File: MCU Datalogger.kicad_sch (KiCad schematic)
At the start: 0 parts

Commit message: imported all needed devices
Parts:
- added BT1: Battery, symbol Device:Battery
- added C1, C2, C3, C4: C, symbol Device:C
- added C5: C_Polarized, symbol Device:C_Polarized
- added D1, D2: LED, symbol Device:LED
- added H1, H2, H3, H4: MountingHole, symbol Mechanical:MountingHole
- added J1, J2: Conn_01x04_Pin, symbol Connector:Conn_01x04_Pin
- added J3: Conn_01x09_Pin, symbol Connector:Conn_01x09_Pin
- added J4: Conn_02x03_Odd_Even, symbol Connector_Generic:Conn_02x03_Odd_Even
- added R1, R2, R3, R4, R5, R6, R7: R, symbol Device:R
- added U1, U2: 24LC1025, symbol Memory_EEPROM:24LC1025
- added U3: ATmega328P-A, Package_QFP:TQFP-32_7x7mm_P0.8mm, symbol MCU_Microchip_ATmega:ATmega328P-A
- added U4: ds1337s+, 21-0041B_8_MXM, symbol 2026-08-13_06-12-53:ds1337s+
- added Y1, Y2: Crystal, symbol Device:Crystal
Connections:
- new net: U3.21 (GND), U3.3 (GND), U3.5 (GND)
- new net: U3.4 (VCC), U3.6 (VCC)
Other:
- company: (none) -> I love KiCAD inc
- title: (none) -> MCU Datalogger w EEPROM & CLK

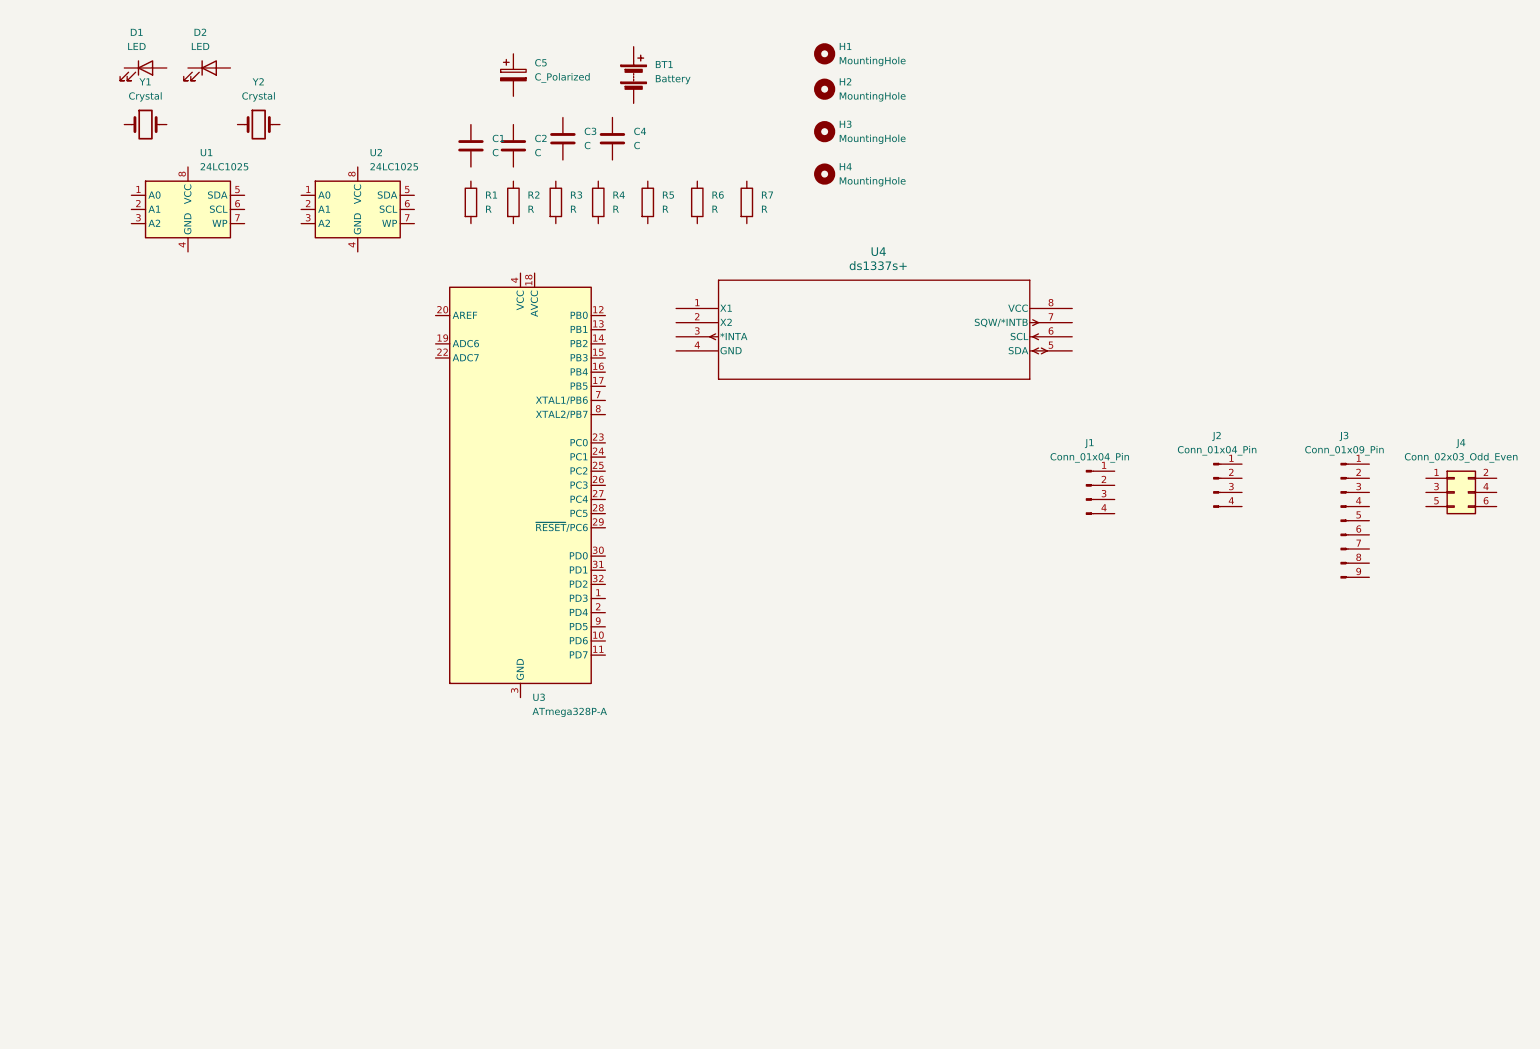
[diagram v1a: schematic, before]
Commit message: added footprints
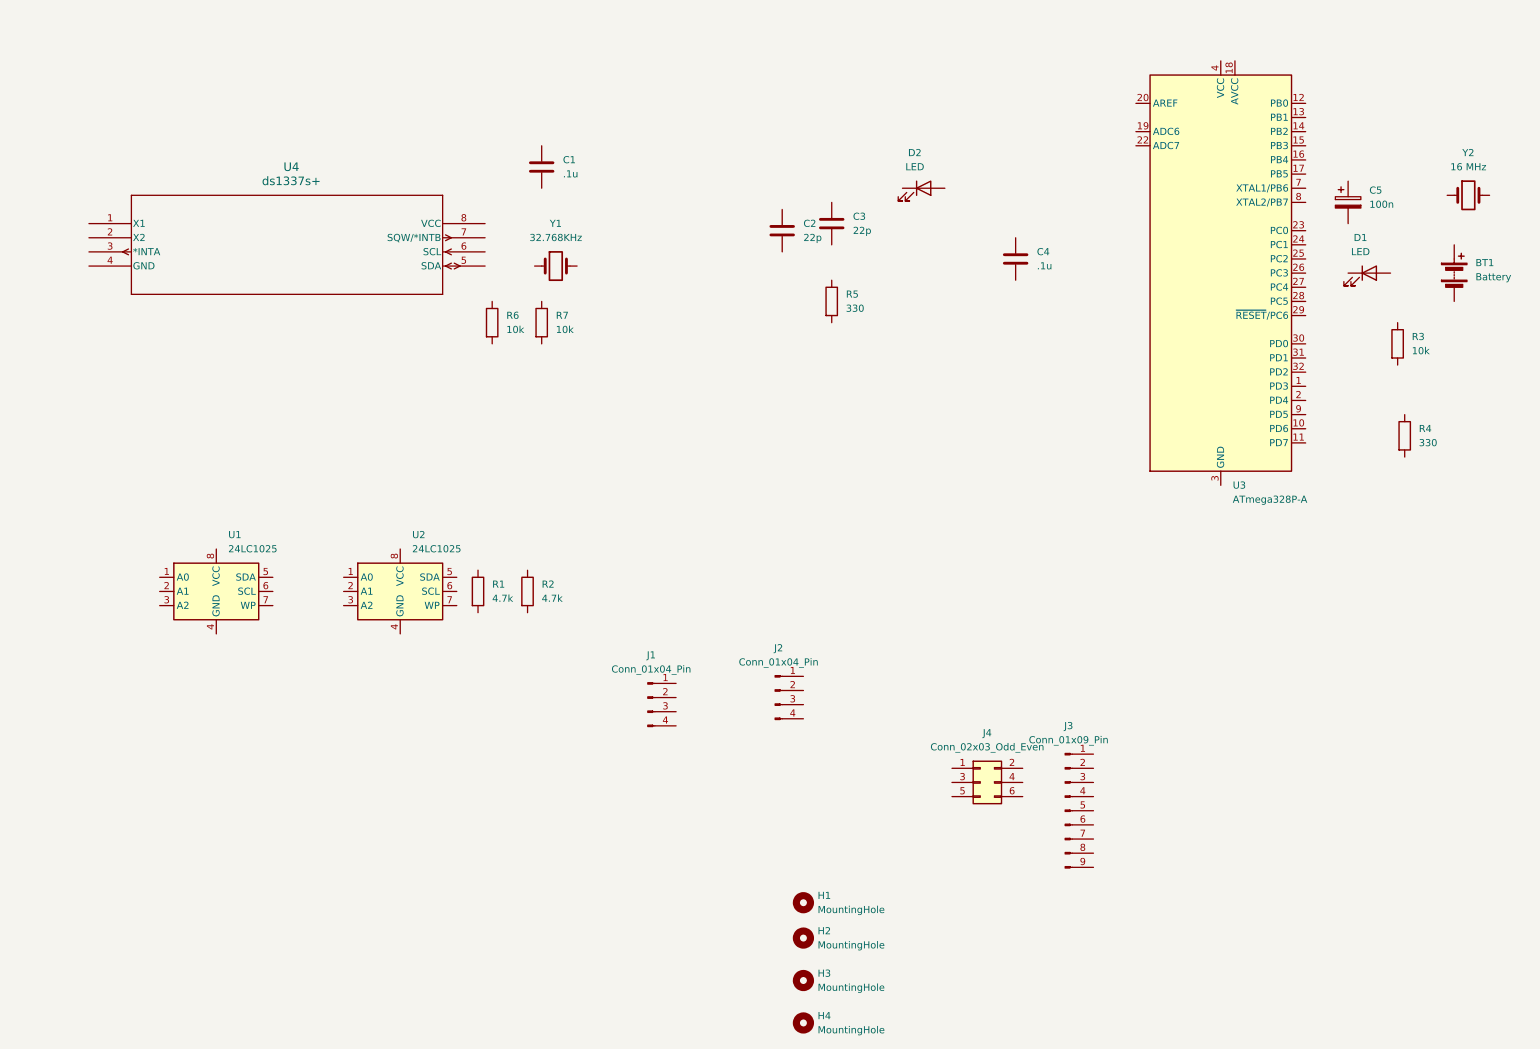
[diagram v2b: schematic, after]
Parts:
- BT1: footprint (none) -> Connector_PinHeader_2.54mm:PinHeader_1x02_P2.54mm_Vertical
- C1, C4: value C -> .1u; footprint (none) -> Capacitor_SMD:C_0805_2012Metric
- C2, C3: value C -> 22p; footprint (none) -> Capacitor_SMD:C_0805_2012Metric
- C5: value C_Polarized -> 100n; footprint (none) -> Capacitor_SMD:C_0805_2012Metric
- D1, D2: footprint (none) -> LED_SMD:LED_0805_2012Metric
- H1, H2, H3, H4: footprint (none) -> MountingHole:MountingHole_2.1mm
- J1, J2: footprint (none) -> Connector_PinHeader_2.54mm:PinHeader_1x04_P2.54mm_Vertical
- J3: footprint (none) -> Connector_PinHeader_2.54mm:PinHeader_1x09_P2.54mm_Vertical
- J4: footprint (none) -> Connector_PinHeader_2.54mm:PinHeader_2x03_P2.54mm_Vertical
- R1, R2: value R -> 4.7k; footprint (none) -> Resistor_SMD:R_0805_2012Metric
- R3, R6, R7: value R -> 10k; footprint (none) -> Resistor_SMD:R_0805_2012Metric
- R4, R5: value R -> 330; footprint (none) -> Resistor_SMD:R_0805_2012Metric
- U1, U2: footprint (none) -> Package_SO:SOIC-8_3.9x4.9mm_P1.27mm
- U4: footprint 21-0041B_8_MXM -> (none)
- Y1: value Crystal -> 32.768KHz; footprint (none) -> Crystal:Crystal_SMD_5032-2Pin_5.0x3.2mm_HandSoldering
- Y2: value Crystal -> 16 MHz; footprint (none) -> Crystal:Crystal_SMD_5032-2Pin_5.0x3.2mm_HandSoldering
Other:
- moved on the sheet: BT1, C1, C2, C3, C4, C5, D1, D2, H1, H2, H3, H4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

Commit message: scematic connections done mostly
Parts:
- removed R3: 10k, Resistor_SMD:R_0805_2012Metric, symbol Device:R
- added R8: 10k, Resistor_SMD:R_0805_2012Metric, symbol Device:R
- U4: footprint (none) -> footprints:21-0041B_8_MXM
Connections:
- net at D1.1 (K): now also R4.1
- net at D1.2 (A): now also BT1.1 (+), C5.1, U3.18 (AVCC), U3.4 (VCC), U3.6 (VCC)
- net at U4.1 (X1): now also Y1.1
- net at U4.2 (X2): now also Y1.2
- net at U4.3 (*INTA): now also R7.2
- net GND: now reaches U4.4 (GND)
- net GND: now also BT1.2 (-), C1.2, C2.2, C3.2, C4.2, C5.2, R4.2, R5.1, U1.4 (GND), U1.7 (WP), U2.2 (A1), U2.4 (GND), U2.7 (WP), U3.21 (GND), U3.3 (GND), U3.5 (GND)
- net SDA: now reaches U4.5 (SDA)
- net SDA: now also R2.2, U1.5 (SDA), U2.5 (SDA), U3.27 (PC4)
- net SCL: now reaches U4.6 (SCL)
- net SCL: now also R1.2, U1.6 (SCL), U2.6 (SCL)
- net at U4.7 (SQW/*INTB): now also R6.2
- net VCC: now reaches U4.8 (VCC)
- net VCC: now also C1.1, R1.1, R2.1, R6.1, R7.1, U1.1 (A0), U1.2 (A1), U1.3 (A2), U1.8 (VCC), U2.1 (A0), U2.3 (A2), U2.8 (VCC), R8.1
- net at Y2.1: now also C3.1, U3.8 (XTAL2/PB7)
- net at Y2.2: now also C2.1, U3.7 (XTAL1/PB6)
- net at D2.1 (K): now also R5.2
- net SCK: now reaches D2.2 (A)
- net SCK: now also U3.17 (PB5), U3.28 (PC5)
- net D3: now reaches U3.1 (PD3)
- net D6: now reaches U3.10 (PD6)
- net D7: now reaches U3.11 (PD7)
- net D8: now reaches U3.12 (PB0)
- net MOSI: now reaches U3.15 (PB3)
- net MISO: now reaches U3.16 (PB4)
- net D4: now reaches U3.2 (PD4)
- net at U3.20 (AREF): now also C4.1
- net RESET: now reaches U3.29 (~{RESET}/PC6)
- net RESET: now also R8.2
- net RX: now reaches U3.30 (PD0)
- net TX: now reaches U3.31 (PD1)
- net D2: now reaches U3.32 (PD2)
- net D5: now reaches U3.9 (PD5)
- no-connect marks 0 -> 8
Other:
- moved on the sheet: BT1, C1, C2, C3, C4, C5, D1, D2, J4, R1, R2, R4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

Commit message: done with labels and connections and net classes
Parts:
- removed J1, J2: Conn_01x04_Pin, Connector_PinHeader_2.54mm:PinHeader_1x04_P2.54mm_Vertical, symbol Connector:Conn_01x04_Pin
- removed J3: Conn_01x09_Pin, Connector_PinHeader_2.54mm:PinHeader_1x09_P2.54mm_Vertical, symbol Connector:Conn_01x09_Pin
- removed J4: Conn_02x03_Odd_Even, Connector_PinHeader_2.54mm:PinHeader_2x03_P2.54mm_Vertical, symbol Connector_Generic:Conn_02x03_Odd_Even
- removed U4: ds1337s+, footprints:21-0041B_8_MXM, symbol 2026-08-13_06-12-53:ds1337s+
- added U4: ds1337s+, footprints:21-0041B_8_MXM, symbol 2026-08-25_23-21-17:ds1337s+
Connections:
- net GND: now also U4.4 (GND)
- net SCL: now also U4.6 (SCL)
- net SDA: now also U4.5 (SDA)
- net VCC: now also BT1.1 (+), C5.1, D1.2 (A), U3.18 (AVCC), U3.4 (VCC), U3.6 (VCC), U4.8 (VCC)
- net at Y1.1: now also U4.1 (X1)
- net at Y1.2: now also U4.2 (X2)
- net at R7.2: now also U4.7 (SQW/*INTB)
- net at R6.2: now also U4.3 (*INTA)
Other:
- added sheet connectors (untitled.kicad_sch)

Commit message: done with more comments
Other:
- note added: "EEPROM"
- note added: "MCU"
- note added: "Mounting"
- note added: "Real Time Clock"
- moved on the sheet: BT1, C2, C3, C4, C5, D1, D2, H1, H2, H3, H4, R4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

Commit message: fixed SCL and SCK
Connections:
- net SCK: no longer U3.28 (PC5)
- net SCL: now also U3.28 (PC5)
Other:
- sheet connectors ports: added SCK; removed none
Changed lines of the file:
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@@
 		)
 	)
-	(label "SCK"
+	(label "SCL"
 		(at 246.38 72.39 0)
 		(effects
@@
 		)
 	)
+	(label "SCK"
+		(at 205.74 134.62 180)
+		(effects
+			(font
+				(size 1.27 1.27)
+			)
+			(justify right bottom)
+		)
+	)
 	(label "MOSI"
 		(at 243.84 44.45 0)
@@
 			)
 		)
+		(pin "SCK" passive
+			(at 205.74 134.62 180)
+			(effects
+				(font
+					(size 1.27 1.27)
+				)
+				(justify left)
+			)
+		)
